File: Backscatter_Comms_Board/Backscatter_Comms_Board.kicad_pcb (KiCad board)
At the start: 2 copper layers, 32.5 x 34.3 mm, 49 parts, among them J1 SPK_IN, J2 Conn_01x11, M1 3SK293, T1 SP-48, U1 ADG919BRMZ, U2 ADG841YKSZ-REEL7, U3 NCS2200SQ2T2G

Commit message: Almost complete :)
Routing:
- net GND: track 40.2 -> 43.8 mm
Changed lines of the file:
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@@
     (thickness 1.6)
     (drawings 17)
-    (tracks 276)
+    (tracks 279)
     (zones 0)
     (modules 49)
@@
   (segment (start 121.158 36.8975) (end 121.158 36.278) (width 0.1524) (layer F.Cu) (net 2) (status 30))
   (segment (start 122.3605 38.1) (end 121.158 36.8975) (width 0.1524) (layer F.Cu) (net 2) (status 30))
+  (segment (start 110.4415 38.366) (end 111.9385 38.366) (width 0.1524) (layer F.Cu) (net 2))
+  (segment (start 112.6115 37.693) (end 112.6115 36.576) (width 0.1524) (layer F.Cu) (net 2))
+  (segment (start 111.9385 38.366) (end 112.6115 37.693) (width 0.1524) (layer F.Cu) (net 2))
   (segment (start 108.038999 41.874199) (end 108.038999 42.570499) (width 0.1524) (layer F.Cu) (net 35) (status 10))
   (segment (start 108.038999 42.570499) (end 108.2675 42.799) (width 0.1524) (layer F.Cu) (net 35))

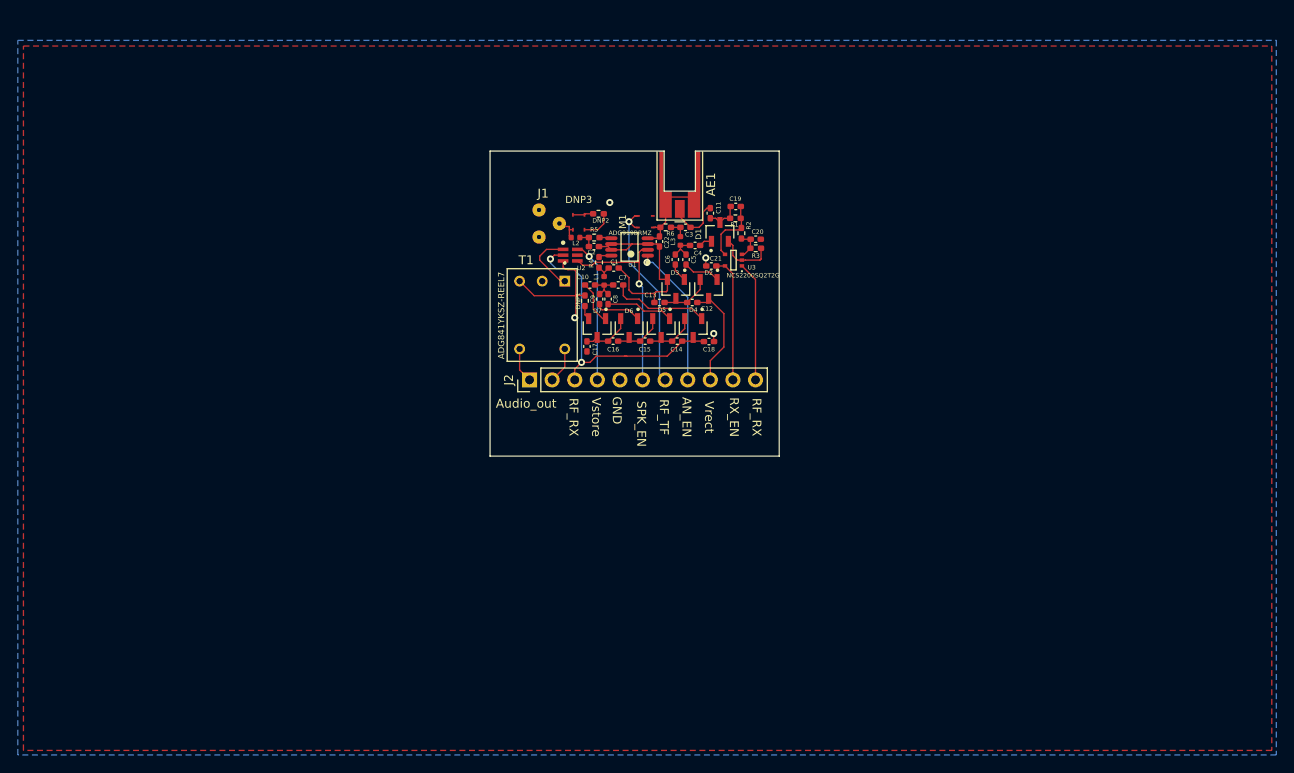
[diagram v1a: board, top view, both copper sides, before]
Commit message: Final v1 backscatter board
Sending to oshpark right after I push!
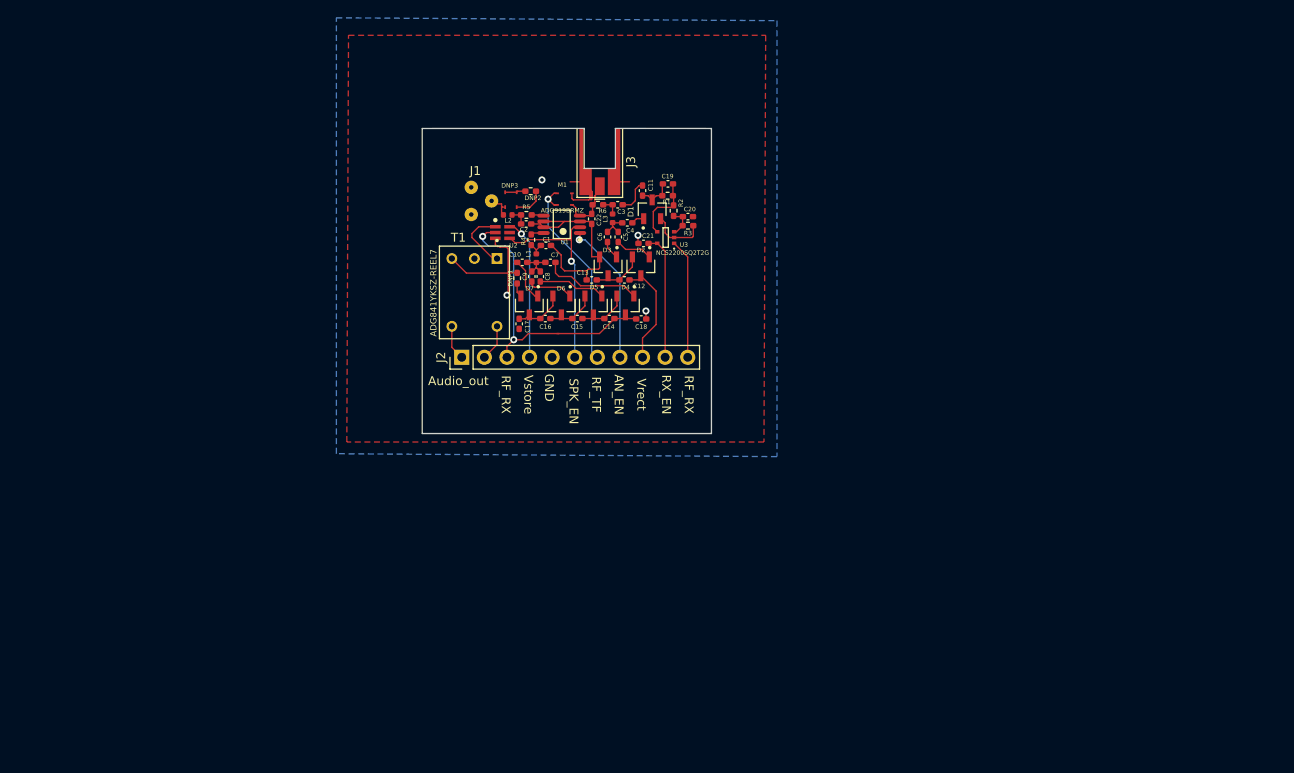
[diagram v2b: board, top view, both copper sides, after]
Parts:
- removed AE1: Antenna_Chip, Connector_Coaxial:MMCX_Molex_73415-0961_Horizontal_0.8mm-PCB
- added J3: Conn_Coaxial_Power, Connector_Coaxial:MMCX_Molex_73415-0961_Horizontal_0.8mm-PCB, F.Cu at (112.2, 30.7)
- R1: value R_US -> 560k
- moved M1 9.44 mm to (108.2, 34.9)
- moved R3 8.03 mm to (122.1, 37.9)
- moved D2 8.03 mm to (116.8, 42.5)
- moved U2 8.03 mm to (101.2, 38.7)
- moved C11 8.03 mm to (117.0, 34.0)
- moved C12 8.03 mm to (114.9, 44.0)
- moved C13 8.03 mm to (111.3, 44.0)
- moved C15 8.03 mm to (109.6, 48.4)
- moved C16 8.03 mm to (106.0, 48.4)
- moved C18 8.03 mm to (116.8, 48.4)
- moved C19 8.03 mm to (119.8, 33.2)
- moved C2 8.03 mm to (103.9, 37.7)
- moved C21 8.03 mm to (117.1, 39.9)
- moved C22 8.03 mm to (111.3, 37.1)
- moved C3 8.03 mm to (114.2, 35.6)
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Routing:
- net GND: track 43.8 -> 50.0 mm
- net Ant: track 11.5 -> 7.07 mm
- net RF_TX: track 22.0 -> 22.6 mm
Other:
- outline, holes or cut-outs redrawn
- rule pad_to_mask_clearance: 0 -> 0.0508

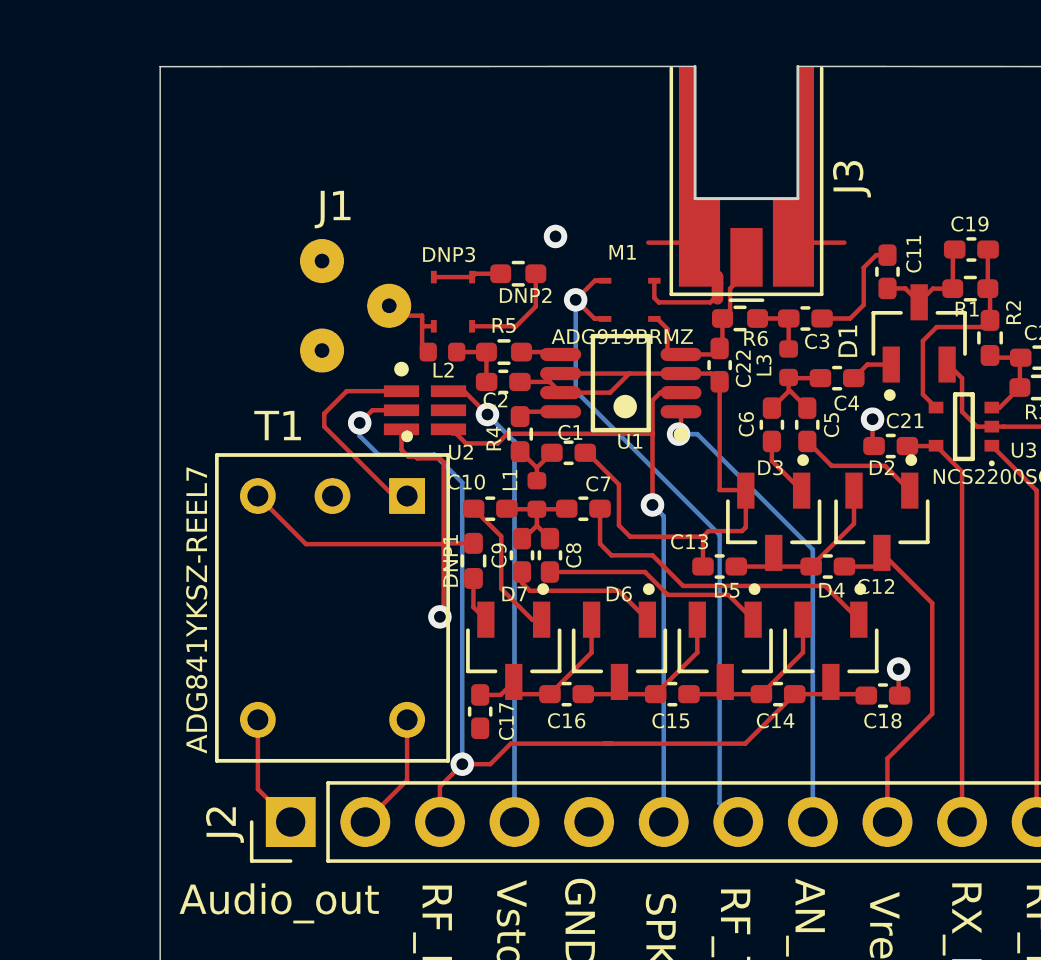
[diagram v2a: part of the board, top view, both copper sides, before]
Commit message: Post mini design review edits
actually ordering this now!
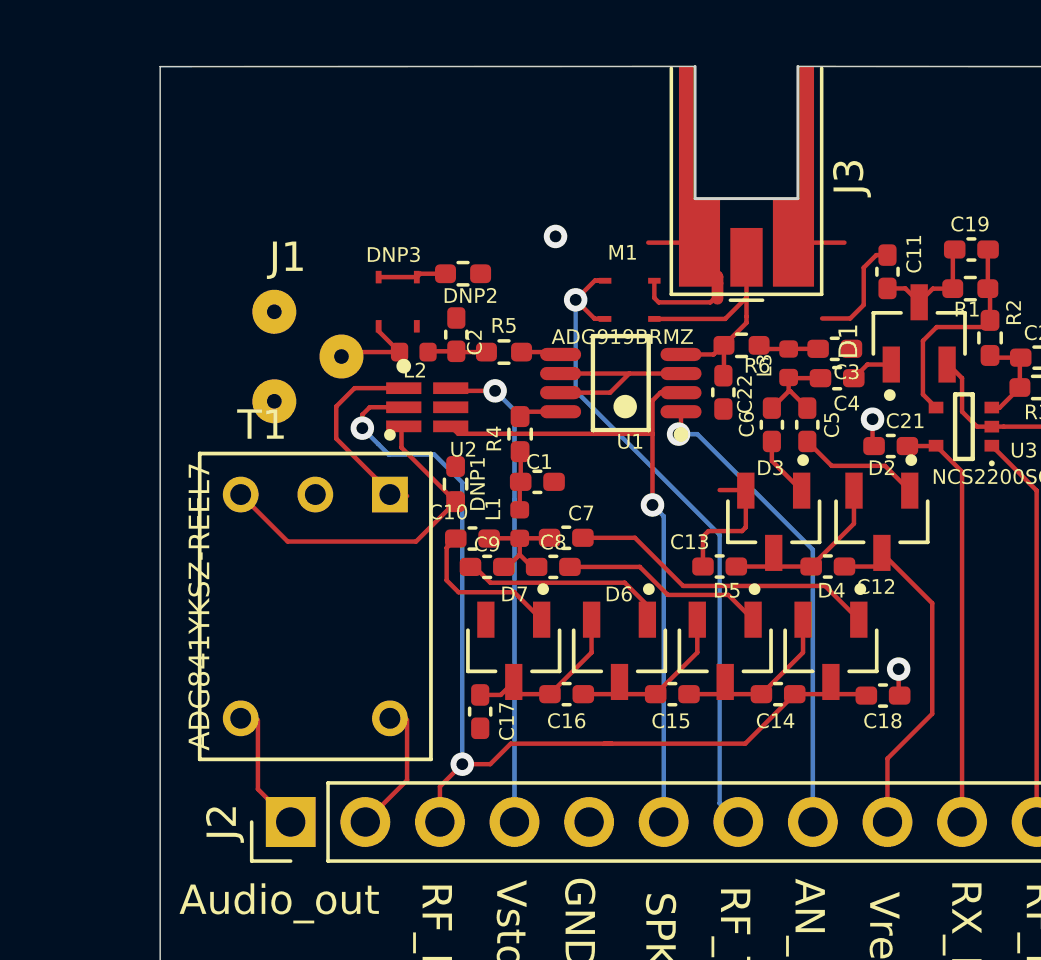
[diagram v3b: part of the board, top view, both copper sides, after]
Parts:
- moved DNP1 2.69 mm to (102.3, 41.2), turned to 270 degrees
- moved J1 2.37 mm to (96.9, 36.9)
- moved C2 2.27 mm to (102.3, 36.1), turned to 90 degrees
- moved DNP2 1.88 mm to (102.5, 34.0)
- moved DNP3 1.88 mm to (100.3, 35.0)
- moved C1 1.45 mm to (105.0, 41.1)
- moved C3 1.44 mm to (115.2, 36.6)
- moved C9 1.25 mm to (103.3, 44.0), turned to 180 degrees
- moved C10 1.18 mm to (102.8, 43.1)
- moved C7 1.15 mm to (106.0, 43.0)
- moved L1 1.15 mm to (104.4, 42.6)
- moved L2 0.98 mm to (100.8, 36.7)
- moved C22 0.94 mm to (111.4, 38.1)
- moved R6 0.92 mm to (112.0, 36.5)
- moved T1 0.59 mm to (97.5, 45.4)
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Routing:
- net GND: track 50.0 -> 32.2 mm
- net Net-(DNP1-Pad2): track 15.7 -> 11.9 mm, vias 1 -> 0
- net Ant: track 7.07 -> 10.4 mm
- net Net-(C9-Pad2): track 5.16 -> 7.05 mm
- net Net-(C10-Pad2): track 4.93 -> 5.75 mm
- net Net-(C8-Pad2): track 7.59 -> 6.98 mm
- net Vstore: track 16.0 -> 16.6 mm
- net Net-(C7-Pad2): track 11.1 -> 10.6 mm
